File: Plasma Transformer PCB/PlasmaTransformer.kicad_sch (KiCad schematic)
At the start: 74 parts, among them J1 Barrel_Jack_MountingPin, J11 Screw_Terminal_01x01, J12 Screw_Terminal_01x01, J2 Conn_01x02_Pin, J3 Conn_Coaxial, J4 Conn_02x04_Odd_Even, J5 Conn_Coaxial, J6 Conn_02x04_Odd_Even, J8 AudioJack3, M1 Fan, Q1 Q_NMOS_Depletion_GDS, SW1 SW_SPDT, T1 BO-02, T2 ZS 1052-S HT(H), U1 LMR51610YDBVR

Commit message: WIP layout
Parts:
- L3: value 56uH -> 22uH; footprint Inductor_SMD:L_Bourns_SRR1210A -> Inductor_SMD:L_Coilcraft_2222SQ-90N; MPN SRR1210-560M -> ETQ-P3M220KVP; Manufacturer Bourns -> Panasonic
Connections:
- net DRAIN: no longer C14.1
- net 12VSW: now reaches C28.1, L3.1, U1.6 (SW)
- net at C1.1, C16.1, C17.1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: now also C14.1
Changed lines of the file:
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@@
-	)
-	(junction
-		(at 251.46 38.1)
-		(diameter 0)
-		(color 0 0 0 0)
 	)
 	(junction
@@
 	(junction
 		(at 233.68 74.93)
+		(diameter 0)
+		(color 0 0 0 0)
+	)
+	(junction
+		(at 252.73 63.5)
 		(diameter 0)
 		(color 0 0 0 0)
@@
 	(wire
 		(pts
+			(xy 252.73 63.5) (xy 269.24 63.5)
+		)
+		(stroke
+			(width 0)
+			(type default)
+		)
+	)
+	(wire
+		(pts
 			(xy 215.9 105.41) (xy 228.6 105.41)
 		)
@@
 	(wire
 		(pts
-			(xy 269.24 38.1) (xy 251.46 38.1)
-		)
-		(stroke
-			(width 0)
-			(type default)
-		)
-	)
-	(wire
-		(pts
 			(xy 146.05 60.96) (xy 146.05 62.23)
 		)
@@
 	(wire
 		(pts
-			(xy 269.24 38.1) (xy 269.24 119.38)
-		)
-		(stroke
-			(width 0)
-			(type default)
-		)
-	)
-	(wire
-		(pts
 			(xy 149.86 74.93) (xy 154.94 74.93)
 		)
@@
 	(wire
 		(pts
-			(xy 252.73 55.88) (xy 252.73 67.31)
+			(xy 252.73 55.88) (xy 252.73 63.5)
 		)
 		(stroke
@@
 	(wire
 		(pts
+			(xy 269.24 63.5) (xy 269.24 119.38)
+		)
+		(stroke
+			(width 0)
+			(type default)
+		)
+	)
+	(wire
+		(pts
 			(xy 113.03 76.2) (xy 109.22 76.2)
 		)
@@
 		(pts
 			(xy 130.81 74.93) (xy 135.89 74.93)
+		)
+		(stroke
+			(width 0)
+			(type default)
+		)
+	)
+	(wire
+		(pts
+			(xy 252.73 63.5) (xy 252.73 67.31)
 		)
 		(stroke
@@
 	(label "VIN"
 		(at 33.02 35.56 0)
+		(effects
+			(font
+				(size 1.27 1.27)
+			)
+			(justify left bottom)
+		)
+	)
+	(label "12VSW"
+		(at 67.31 71.12 0)
 		(effects
 			(font
@@
 			)
 		)
-		(property "Value" "56uH"
+		(property "Value" "22uH"
 			(at 75.184 73.406 90)
 			(effects
@@
 			)
 		)
-		(property "Footprint" "Inductor_SMD:L_Bourns_SRR1210A"
+		(property "Footprint" "Inductor_SMD:L_Coilcraft_2222SQ-90N"
 			(at 74.93 71.12 0)
 			(effects
@@
 			)
 		)
-		(property "MPN" "SRR1210-560M"
+		(property "MPN" "ETQ-P3M220KVP"
 			(at 74.93 71.12 90)
 			(effects
@@
 			)
 		)
-		(property "Manufacturer" "Bourns"
+		(property "Manufacturer" "Panasonic"
 			(at 74.93 71.12 90)
 			(effects

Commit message: improvements to ease of assembly, increased use of solid pours, layout complete, 1st DRC check complete.
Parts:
- removed D4: D, Diode_SMD:D_SOD-323, symbol Device:D
- added J10, J13, J14, J15, J16, J17, J18, J19, J20, J21, J7, J9: Conn_01x01_Socket, ALibrary:H8501-05, symbol Connector:Conn_01x01_Socket
- C2: footprint Capacitor_THT:CP_Radial_D10.0mm_P5.00mm -> ALibrary:CP_Elec_16x17.5_FK_Series; MPN ECA-1JHG331 -> EEV-FK1K331M; Voltage 63V -> 80V
- D1: footprint Diode_SMD:D_SOD-323_HandSoldering -> Diode_SMD:D_SMA; MPN TDZ10J,115 -> SMAZ10-13-F
- J4, J6: footprint Connector_PinHeader_2.54mm:PinHeader_2x04_P2.54mm_Vertical -> Connector_PinHeader_2.54mm:PinHeader_2x04_P2.54mm_Vertical_SMD; MPN TSW-104-07-F-D -> TSM-104-01-L-DV-P-TR
- L3: footprint Inductor_SMD:L_Coilcraft_2222SQ-90N -> ALibrary:L_Pana_PCC-KVP_5.5x5mm
- RV1: footprint ALibrary:SMC10H04-102A2020MTA -> ALibrary:Bourns-Potentiometer-PTD902-2; MPN SMC10H04-102A2020MTA -> PTD902-1015K-B102
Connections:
- net at RV1.1: now also R4.1; no longer R3.2
- net at RV1.3: now also R3.2; no longer R4.1
- net FEEDBACK: now reaches C1.2, C16.2, C17.2, C18.2, C19.2, C20.2, C23.2, D6.1 (K), D8.2 (A), H1.1, J6.1 (Pin_1), J6.3 (Pin_3), J6.5 (Pin_5), J6.7 (Pin_7), R6.2
- net FEEDBACK: now also J13.1 (Pin_1), J15.1 (Pin_1), J17.1 (Pin_1), J19.1 (Pin_1), J21.1 (Pin_1), J9.1 (Pin_1)
- net RF-NODE: now reaches C1.1, C14.1, C16.1, C17.1, C18.1, C19.1, C20.1, J12.1 (Pin_1)
- net RF-NODE: now also J10.1 (Pin_1), J14.1 (Pin_1), J16.1 (Pin_1), J18.1 (Pin_1), J20.1 (Pin_1), J7.1 (Pin_1)
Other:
- note added: "POWER INPUT (12.5-60V)"
- note removed: "POWER INPUT (12.5-65V)"
- moved on the sheet: C1, C16, C17, C18, C19, C20, C25, C26, C27, C28, J11, J12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

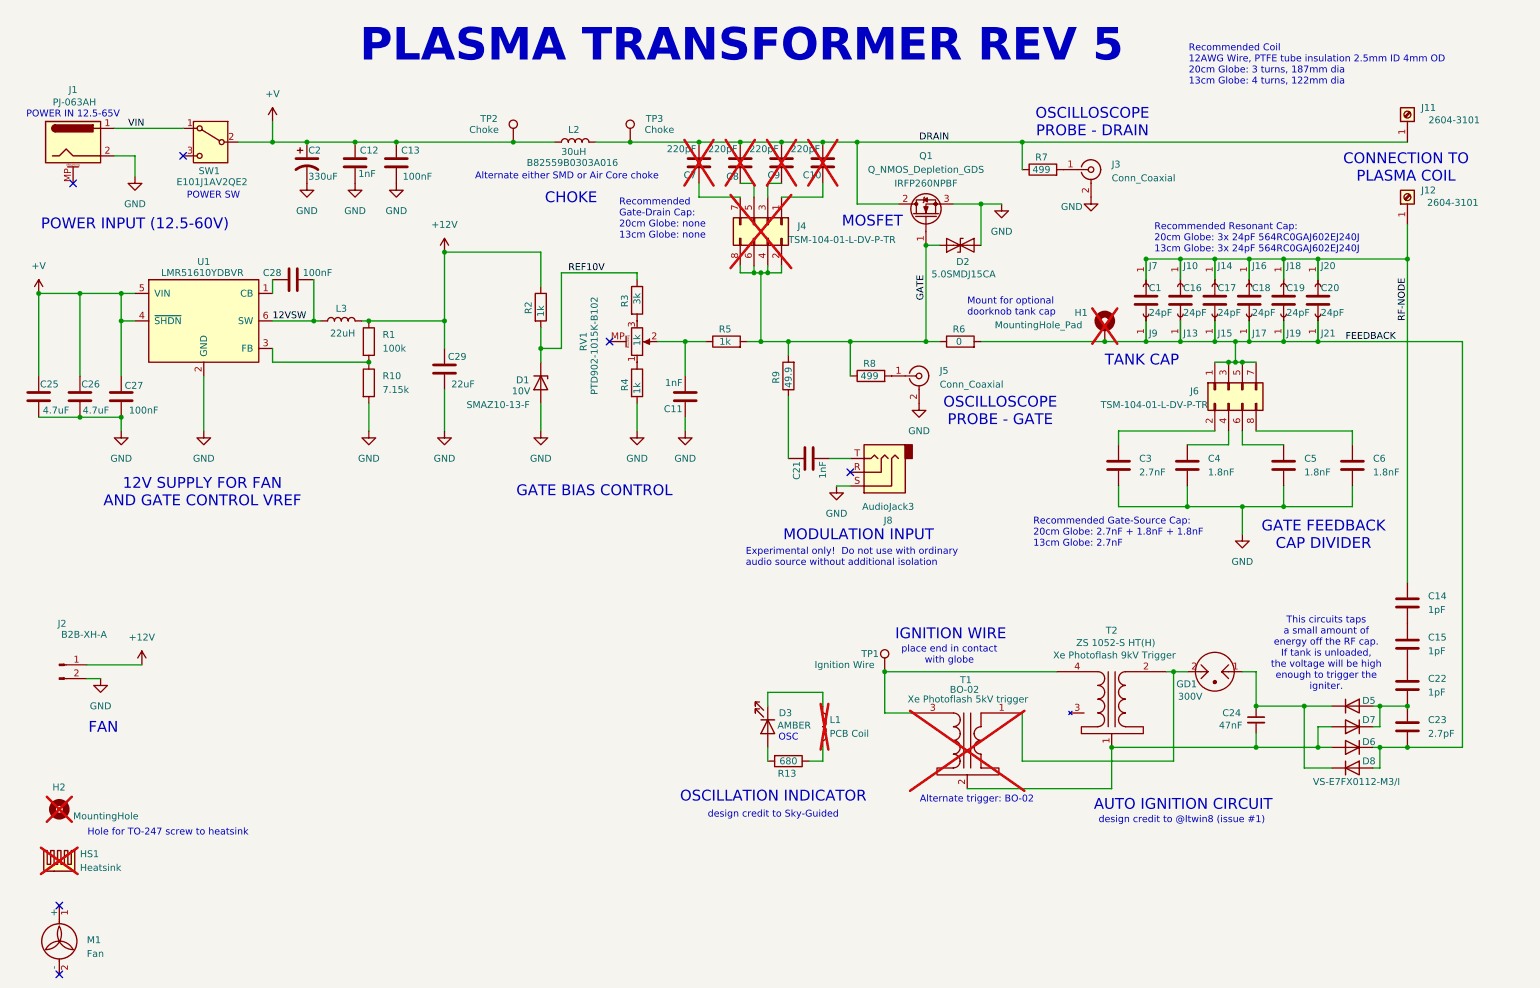
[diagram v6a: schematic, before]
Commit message: clean up for manufacturing
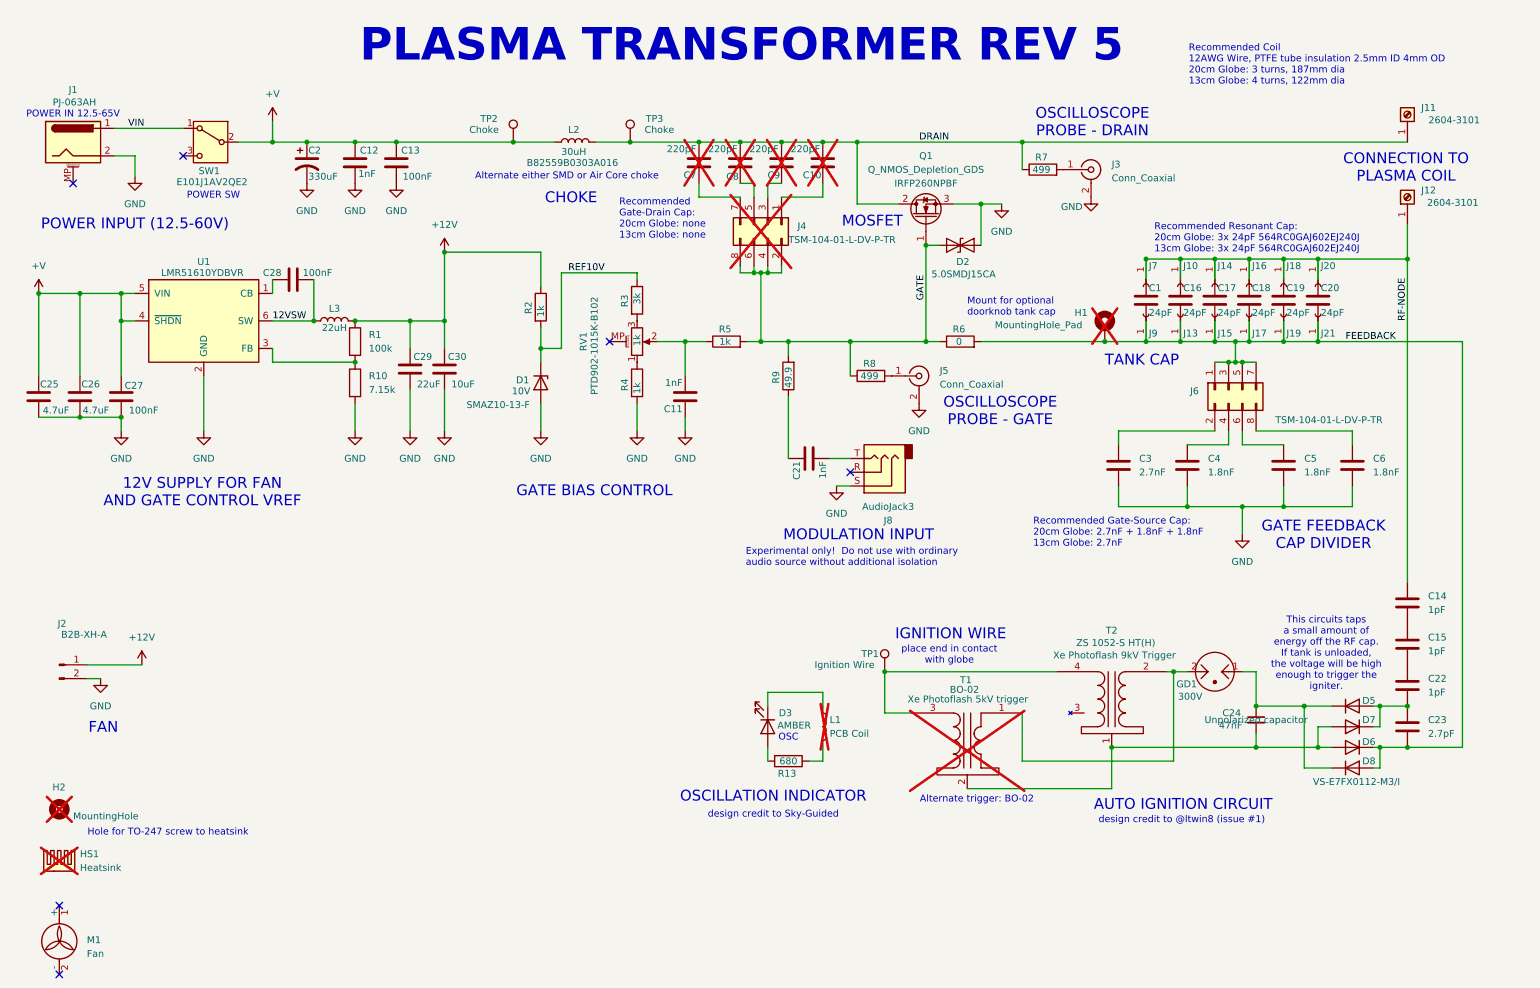
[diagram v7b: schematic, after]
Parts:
- added C30: 10uF, Capacitor_SMD:C_0805_2012Metric, symbol Device:C
- C25, C26: MPN (none) -> CL32B475KCVZW6E; Manufacturer (none) -> Samsung
- J10, J13, J14, J15, J16, J17, J18, J19, J20, J21, J7, J9: MPN (none) -> H8501-05; Manufacturer (none) -> Harwin
- J2: footprint Connector_JST:JST_XH_B2B-XH-AM_1x02_P2.50mm_Vertical -> Connector_JST:JST_XH_B2B-XH-A_1x02_P2.50mm_Vertical
- R1: MPN (none) -> RC0805FR-07100KL; Manufacturer (none) -> Yageo
- R10: MPN (none) -> RC0805FR-077K15L; Manufacturer (none) -> Yageo
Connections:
- net +12V: now also C30.2
- net GND: now also C30.1
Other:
- moved on the sheet: C29, L3, R1, R10

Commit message: Clean up, silkscreens, BOM cleanup, title blocks, fab notes, generate manufacturing files
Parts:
- C1, C16, C17, C18, C19, C20: Dielectric (none) -> NP0; Voltage (none) -> 6000V
- C10, C7, C8, C9: Dielectric (none) -> C0G; Voltage (none) -> 1000V
- C11, C12, C14, C15, C21, C22, C23: Dielectric (none) -> C0G; Voltage (none) -> 2000V
- C13: Dielectric (none) -> X7R; Voltage (none) -> 1000V
- C2: Dielectric (none) -> Al Elec
- C24: Dielectric (none) -> X7R; Voltage (none) -> 500V
- C3: Dielectric (none) -> X7R; Voltage (none) -> 2000V
- C4, C5, C6: Dielectric (none) -> NP0; Voltage (none) -> 500V
- D1: value 10V -> 10V Zener
- D2: value 5.0SMDJ15CA -> 15V TVS
- D5, D6, D7, D8: Voltage (none) -> 1200V
- GD1: value 300V -> 300V GDT
- H1: value MountingHole_Pad -> Pad_Doorknob_Cap
- H2: value MountingHole -> Hole_Heatsink_Screw
- HS1: MPN (none) -> SK 594 37,5 AL; Manufacturer (none) -> Fischer; now fitted
- M1: MPN AFB0924VH-R00 -> AFB0912VHD-F00
- R13, R2, R3, R4, R5, R6, R7, R8, R9: Tolerance (none) -> 1%
- TP1, TP2, TP3: now not fitted
